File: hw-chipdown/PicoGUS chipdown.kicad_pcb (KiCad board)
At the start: 4 copper layers, 102.9 x 96.7 mm, 99 parts, among them J1 Bus_ISA_8bit, J10 Conn_01x02_Pin, J2 DEBUG, J3 IRQDMA_JP, J4 UART_TX, J5 USB_A - joy, J6 USB_B_Micro - program, J7 3.5mm TRS, J8 Wavetable, J9 3.5mm TRS, Q1 AO3401A, SW1 SW_Push, U1 SN74CB3T3257, U10 PCM5100, U11 W25Q128JVS, U12 RP2040, U13 M62429L, U2 SN74CB3T3257, U3 74AHC14, U4 74LVC00, U5 74LVC00, U6 74LVC2G06, U7 SN74CB3T3245, U8 APS6404L-3SQR-SN, U9 AMS1117-3.3_SOT223, Y1 ABLS-12.000MHZ-B4-T

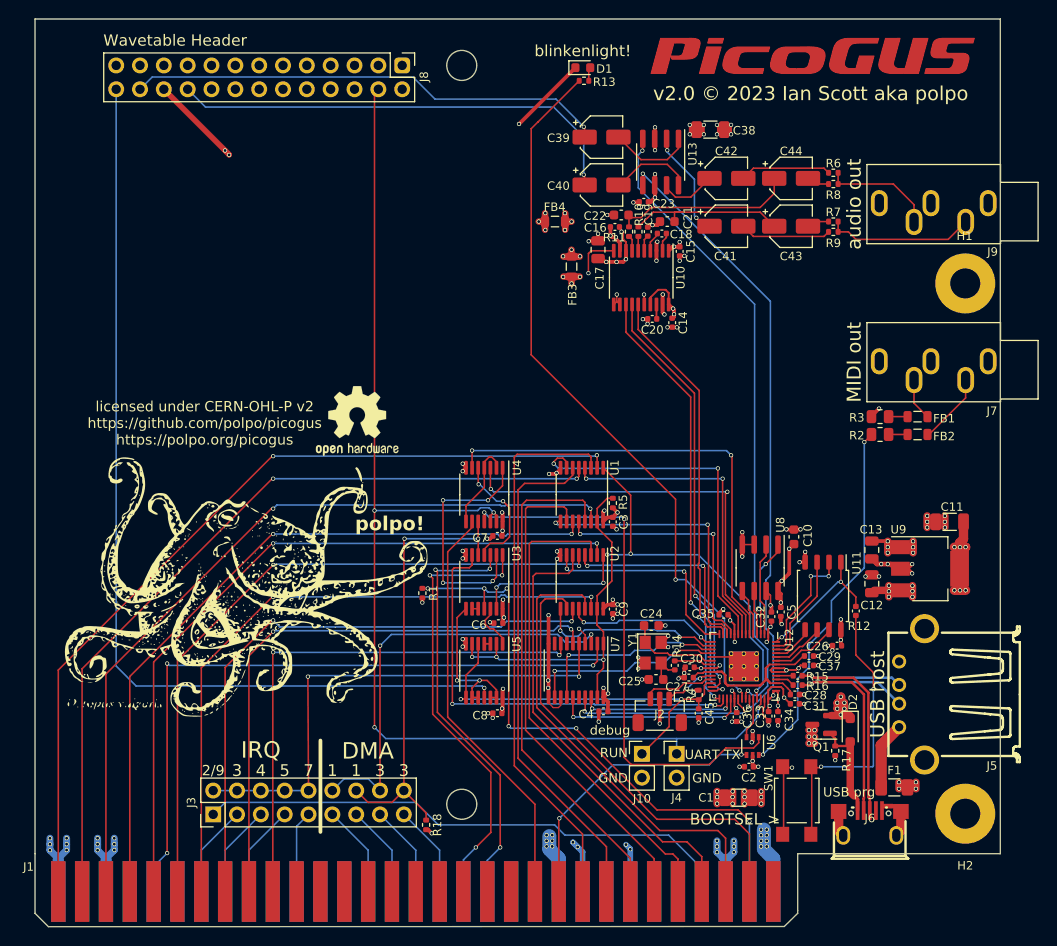
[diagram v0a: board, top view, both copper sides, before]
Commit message: v2.0 with 0805 components
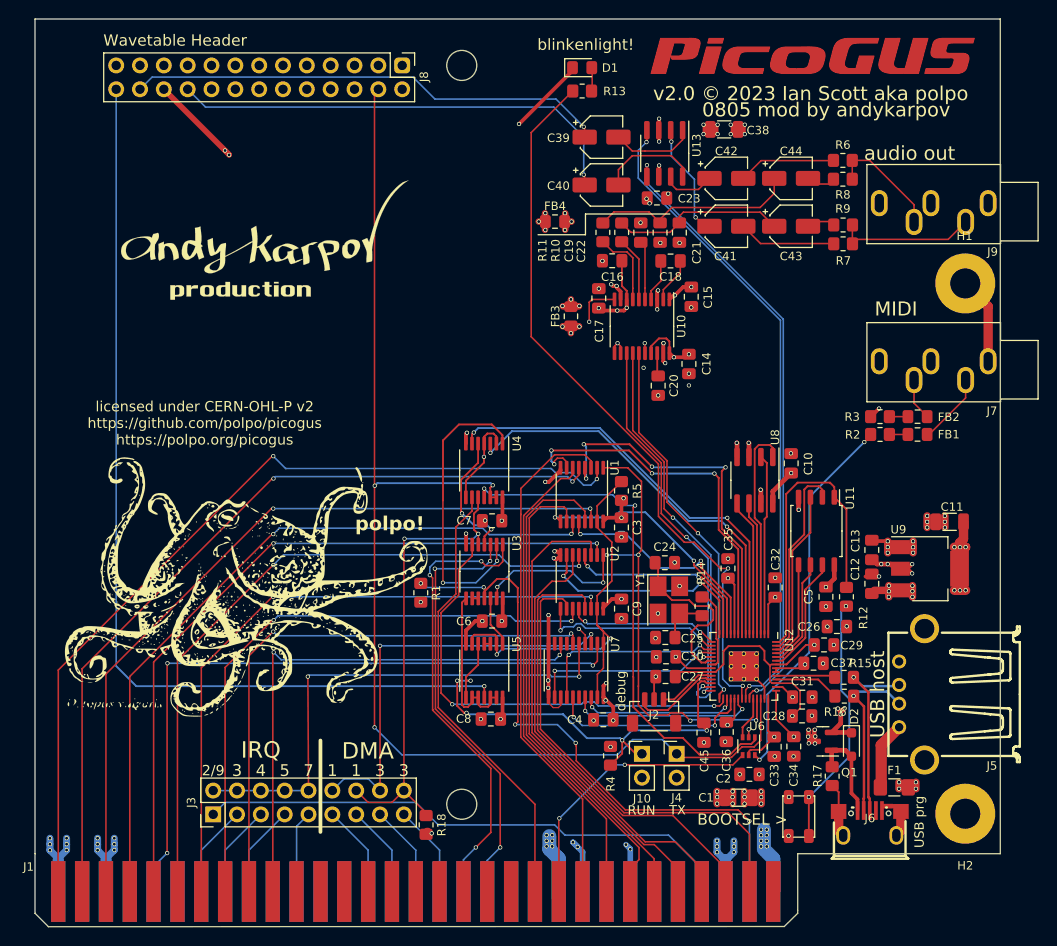
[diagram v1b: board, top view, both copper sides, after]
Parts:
- removed REF**: OSHW-Logo2_9.8x8mm_SilkScreen, Symbol:OSHW-Logo2_9.8x8mm_SilkScreen
- added G***: LOGO, footprints:andy_karpov_logo4_silk, F.Cu at (141.0, 62.9)
- C10, C21, C22, C24, C25: footprint Capacitor_SMD:C_0603_1608Metric -> Capacitor_SMD:C_0805_2012Metric_Pad1.18x1.45mm_HandSolder
- C12, C13, C17: footprint Capacitor_SMD:C_0805_2012Metric -> Capacitor_SMD:C_0805_2012Metric_Pad1.18x1.45mm_HandSolder
- C14, C15, C16, C18, C19, C2, C20, C23, C26, C27, C28, C29, C3, C30, C31, C32, C33, C34, C35, C36, C37, C4, C45, C5, C6, C7, C8, C9: footprint Capacitor_SMD:C_0402_1005Metric -> Capacitor_SMD:C_0805_2012Metric_Pad1.18x1.45mm_HandSolder
- D1: footprint LED_SMD:LED_0603_1608Metric -> LED_SMD:LED_0805_2012Metric_Pad1.15x1.40mm_HandSolder
- F1: footprint Fuse:Fuse_1206_3216Metric -> Fuse:Fuse_1206_3216Metric_Pad1.42x1.75mm_HandSolder
- FB1, FB2, FB3, FB4: footprint Inductor_SMD:L_0805_2012Metric -> Inductor_SMD:L_0805_2012Metric_Pad1.15x1.40mm_HandSolder
- R1, R10, R11, R13, R17, R18, R4, R5, R6, R7, R8, R9: footprint Resistor_SMD:R_0402_1005Metric -> Resistor_SMD:R_0805_2012Metric_Pad1.20x1.40mm_HandSolder
- R12, R14, R15, R16: footprint Capacitor_SMD:C_0402_1005Metric -> Resistor_SMD:R_0805_2012Metric_Pad1.20x1.40mm_HandSolder
- R2, R3: footprint Resistor_SMD:R_0805_2012Metric -> Resistor_SMD:R_0805_2012Metric_Pad1.20x1.40mm_HandSolder
- SW1: footprint Button_Switch_SMD:SW_SPST_TL3305A -> footprints:SW_SPST_PTS810_handsoldering
- Y1: footprint Crystal:Crystal_SMD_3225-4Pin_3.2x2.5mm -> Crystal:Crystal_SMD_3225-4Pin_3.2x2.5mm_HandSoldering
- moved R4 11.4 mm to (177.9, 117.8)
- moved U8 9.35 mm to (193.2, 88.5)
- moved C10 7.84 mm to (197.1, 86.7)
- moved C20 7.14 mm to (182.9, 78.4), turned to -90 degrees
- moved U11 6.96 mm to (199.8, 93.9)
- moved R14 6.93 mm to (187.6, 101.9)
- moved C24 6.85 mm to (183.6, 97.3)
- moved Y1 5.87 mm to (184.1, 101.2)
- moved FB3 5.29 mm to (173.6, 71.0)
- moved C17 5.19 mm to (176.6, 69.1)
- moved U10 5.19 mm to (181.2, 72.1)
- moved R16 5.11 mm to (202.8, 111.5)
- moved C5 5.07 mm to (200.8, 100.9)
- moved C15 4.99 mm to (186.5, 68.9)
- moved C35 4.96 mm to (190.4, 97.9), turned to 90 degrees
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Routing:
- net /RP2040/QSPI_SS: track 14.9 -> 33.5 mm, vias 2 -> 0
- net GND: track 190.3 -> 172.7 mm, vias 110 -> 96
- net ~{SPI_CS}: track 9.67 -> 23.2 mm, vias 2 -> 0
- net /USB_D-: track 29.7 -> 18.2 mm
- net /USB_D+: track 30.1 -> 20.2 mm
- net RUN: track 43.3 -> 53.2 mm, vias 2 -> 5
- net SPI_TX: track 4.75 -> 14.6 mm
- net SPI_SCK: track 4.71 -> 14.3 mm
- net SPI_RX: track 9.99 -> 19.2 mm
- net ADS: track 56.0 -> 65.2 mm, vias 5 -> 6
- net /RP2040/XIN: track 9.41 -> 18.3 mm
- net +1V1: track 18.9 -> 27.6 mm, vias 0 -> 2
- net +3V3: track 75.4 -> 84.0 mm, vias 50 -> 37
- net /RP2040/QSPI_SD1: track 12.8 -> 21.2 mm, vias 2 -> 0
- net AD0: track 33.2 -> 40.1 mm, vias 2 -> 4
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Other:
- board text added: "0805 mod by andykarpov"
- board text added: "MIDI"
- board text added: "TX"
- board text added: "thanks to: 48kRAM Aaron Giles Adrian Black Chrissy Claude Schwarz deck/scoopex djh0ffman FireTwoOneNine foone FreddyV furan Graham Sanderson HeathenUK indigoparadox Jim Leonard Jonathan Campbell Konrad Beckmann Kalantaj"
- board text removed: "GND"
- board text removed: "MIDI out"
- board text removed: "UART TX"
- board text removed: "thanks to: 48kRAM Aaron Giles Adrian Black Chrissy Claude Schwarz deck/scoopex djh0ffman FireTwoOneNine foone FreddyV furan Graham Sanderson HeathenUK indigoparadox Jim Leonard Jonathan Campbell Konrad Beckmann"
